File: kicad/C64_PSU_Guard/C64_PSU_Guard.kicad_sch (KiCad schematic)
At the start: 46 parts, among them J1 PSU_IN, J2 DRIVE, J3 UFI_LINK, Q1 AO3401A, Q2 2N7002, Q3 AO3401A, Q4 2N7002, U1 TPS25921ADR, U2 TPS25921ADR

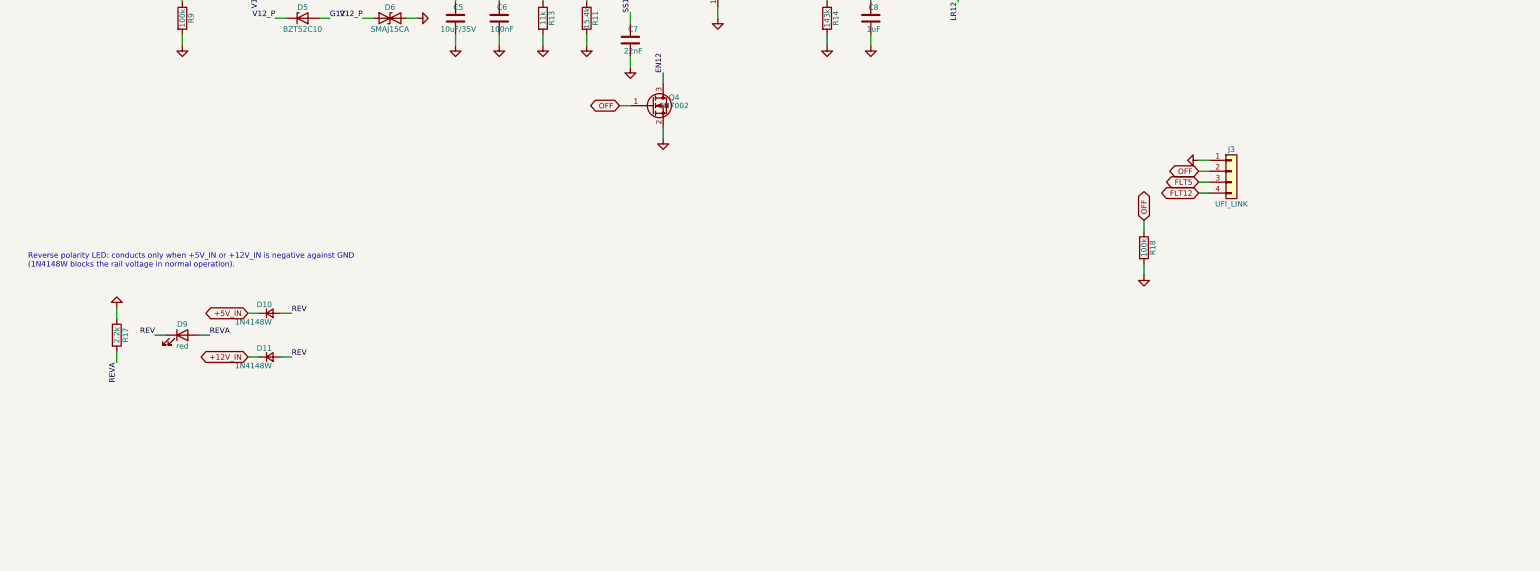
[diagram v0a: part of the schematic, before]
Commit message: C64 PSU Guard: external LED header J4 (2x5, one pair per LED with own series resistor R19-R23, parallel to the on-board LEDs), J3 ERR5/ERR12 now open-drain outputs through 2N7002 inverters Q5/Q6 (the eFuse FLT nodes sit at rail voltage via the red LED chains, up to 12 V, so they must not reach a 3.3 V input directly; high = fault or guard unpowered), README: mapping to UFI Headless J9 (PB6/PB7 with their 2.2k pull-ups, PE0 as OFF); headers 0.5/1 mm off the edge, island vias for pour fragments, GND single-spoke rule for all GND pads, 40 router passes; ERC/DRC 0, fab files regenerated
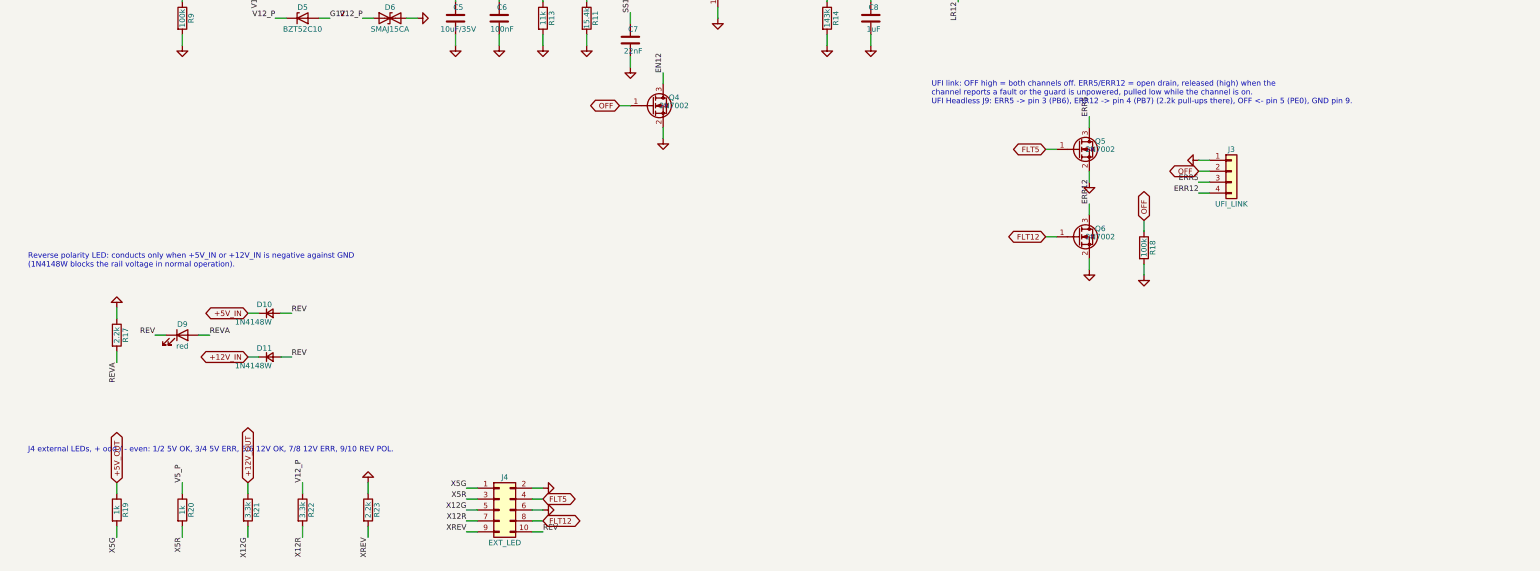
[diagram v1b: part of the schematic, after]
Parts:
- added J4: EXT_LED, Connector_PinHeader_2.54mm:PinHeader_2x05_P2.54mm_Vertical, symbol Connector_Generic:Conn_02x05_Odd_Even
- added Q5, Q6: 2N7002, Package_TO_SOT_SMD:SOT-23, symbol Transistor_FET:2N7002
- added R19, R20: 1k, Resistor_SMD:R_0603_1608Metric, symbol Device:R
- added R21, R22: 3.3k, Resistor_SMD:R_0603_1608Metric, symbol Device:R
- added R23: 2.2k, Resistor_SMD:R_0603_1608Metric, symbol Device:R
- J3: Note reserve: OFF high = both channels off (100k pull-down), FLT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 -> 1 GND, 2 OFF (high = both channels off, 100k pull-down), 3 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
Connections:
- net +12V_OUT: now also R21.1
- net +5V_OUT: now also R19.1
- net FLT12: now also J4.8 (Pin_8), Q6.1 (G); no longer J3.4 (Pin_4)
- net FLT5: now also J4.4 (Pin_4), Q5.1 (G); no longer J3.3 (Pin_3)
- net GND: now also J4.2 (Pin_2), J4.6 (Pin_6), Q5.2 (S), Q6.2 (S), R23.1
- net REV: now also J4.10 (Pin_10)
- net V12_P: now also R22.1
- net V5_P: now also R20.1
- new net ERR12: J3.4 (Pin_4), Q6.3 (D)
- new net ERR5: J3.3 (Pin_3), Q5.3 (D)
- new net X12G: J4.5 (Pin_5), R21.2
- new net X12R: J4.7 (Pin_7), R22.2
- new net X5G: J4.1 (Pin_1), R19.2
- new net X5R: J4.3 (Pin_3), R20.2
- new net XREV: J4.9 (Pin_9), R23.2
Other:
- note added: "J4 external LEDs, + odd / - even: 1/2 5V OK, 3/4 5V ERR, 5/6 12V OK, 7/8 12V ERR, 9/10 REV POL."
- note added: "UFI link: OFF high = both channels off. ERR5/ERR12 = open drain, released (high) when the channel reports a fault or the guard is unpowered, pulled low while the channel is on. UFI Headless J9: ERR5 -> pin 3 (PB6), ERR12 -> pin 4 (PB7) (2.2k pull-ups there), OFF <- pin 5 (PE0), GND pin 9."

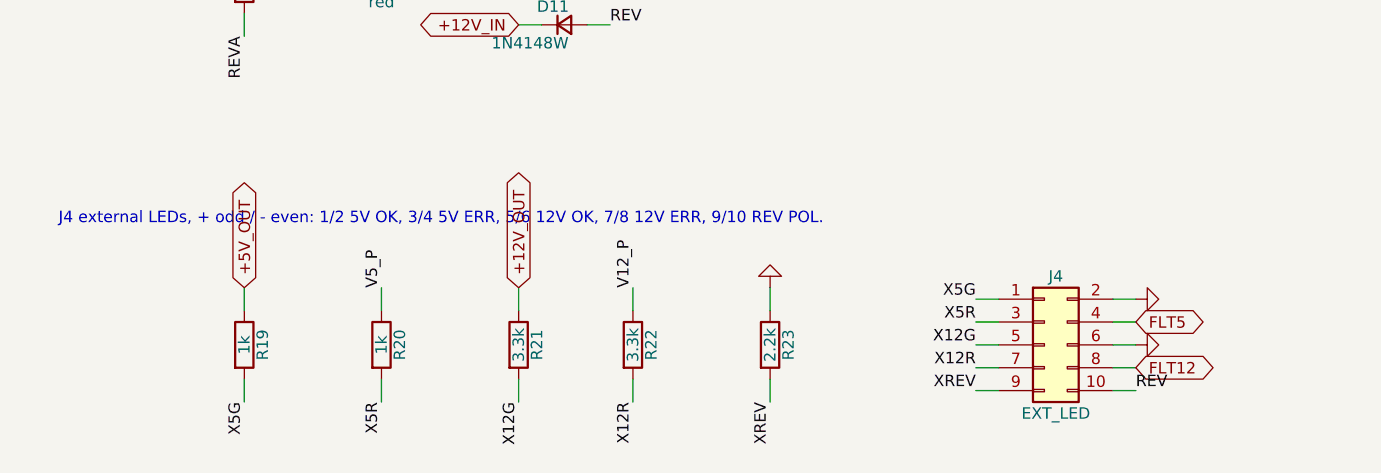
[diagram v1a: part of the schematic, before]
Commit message: C64 PSU Guard: one external fault LED instead of the 2x5 LED header - J4 1x2 (1 = +, 2 = -), 1k from the protected 5 V input, cathode through a 1N4148W diode OR (D12/D13) into both eFuse FLT outputs: on while either channel is switched off; README, fab files regenerated, ERC/DRC 0
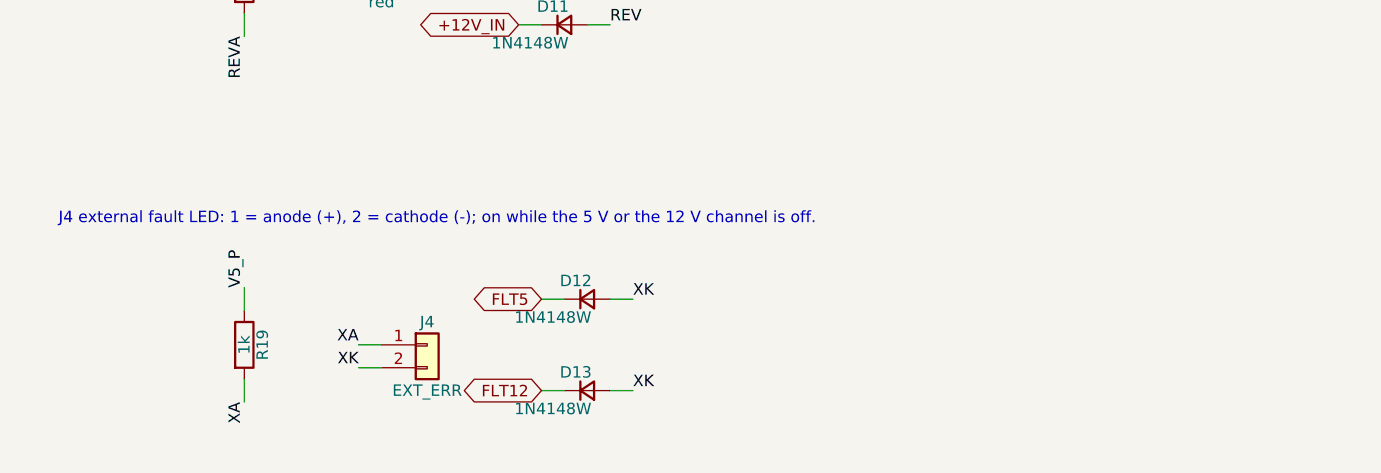
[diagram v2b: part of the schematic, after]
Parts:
- removed R20: 1k, Resistor_SMD:R_0603_1608Metric, symbol Device:R
- removed R21, R22: 3.3k, Resistor_SMD:R_0603_1608Metric, symbol Device:R
- removed R23: 2.2k, Resistor_SMD:R_0603_1608Metric, symbol Device:R
- added D12, D13: 1N4148W, Diode_SMD:D_SOD-123, symbol Device:D_Small
- J4: value EXT_LED -> EXT_ERR; footprint Connector_PinHeader_2.54mm:PinHeader_2x05_P2.54mm_Vertical -> Connector_PinHeader_2.54mm:PinHeader_1x02_P2.54mm_Vertical; symbol Connector_Generic:Conn_02x05_Odd_Even -> Connector_Generic:Conn_01x02; LCSC C2894971 -> C54620389; Note external LEDs, + odd / - even: 5V OK, 5V ERR, 12V OK, 12V E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 -> external fault LED, 1 = + (anode), 2 = - (cathode), ~2.5 mA
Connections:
- net +5V_OUT: no longer R19.1
- net FLT12: now also D13.1 (K); no longer J4.8 (Pin_8)
- net FLT5: now also D12.1 (K); no longer J4.4 (Pin_4)
- net GND: no longer J4.2 (Pin_2), J4.6 (Pin_6)
- net REV: no longer J4.10 (Pin_10)
- net V5_P: now also R19.1
- removed net X12G: J4.5 (Pin_5)
- removed net X12R: J4.7 (Pin_7)
- net X5G renamed XA
- removed net X5R: J4.3 (Pin_3)
- removed net XREV: J4.9 (Pin_9)
- new net XK: D12.2 (A), D13.2 (A), J4.2 (Pin_2)
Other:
- note added: "J4 external fault LED: 1 = anode (+), 2 = cathode (-); on while the 5 V or the 12 V channel is off."
- note removed: "J4 external LEDs, + odd / - even: 1/2 5V OK, 3/4 5V ERR, 5/6 12V OK, 7/8 12V ERR, 9/10 REV POL."

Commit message: C64 PSU Guard v0.2 stage G1 (schematic), review of 2026-10-24: (1) J1 PSU IN is a keyed JST XH B4B-XH-A (LCSC C144395, pin order 1 +5V, 2/3 GND, 4 +12V as on UFI J17/J3) instead of the unkeyed pin header that could be plugged 180 deg rotated (12 V on the 5 V channel, D2 SMF5.0CA would burn); D2 stays the 5 V clamp. (2) D6 SMAJ15CA (VC 24.4 V, above the TPS25921A IN rating 20 V / 22 V for 10 ms) replaced by the unidirectional SMAJ13A (Diodes SMAJ13A-13-F, C110519: VRWM 13 V, VBR 14.4-15.9 V at 1 mA, VC 21.5 V at 18.6 A), drawn as D_Zener so the polarity is visible: pin 1 = cathode = V12_P, pin 2 = GND, D_SMA pad 1 = cathode band. (4) R20/R21 100k (C25803) from FLT5 to V5_P and FLT12 to V12_P, parallel to the red LED chains, so FLT and the Q5/Q6 gates have a defined level; numbered last, v0.1 references unchanged. (5) J3 UFI link is a JST XH B4B-XH-A as well, pin order 1 GND, 2 OFF, 3 ERR5, 4 ERR12 = UFI v1.0 J20 GUARD (netlist of kicad/UFI_Headless: J20.1 GND, J20.2 GUARD_OFF_J <- PG7, J20.3 GUARD_ERR5_J -> PG8, J20.4 GUARD_ERR12_J -> PC9), 1:1 XH cable; schematic notes now name J20 instead of the removed J9. PLAN.md with the stages G1-G3. ERC --severity-all 0 errors / 0 warnings. The board follows in stage G2 (layout regenerated from the scripts), so no DRC in this stage.
Claude-Session: https://claude.ai/code/session_014MdzrcyXuayppPHbfEjUrw
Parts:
- added R20, R21: 100k, Resistor_SMD:R_0603_1608Metric, symbol Device:R
- D6: value SMAJ15CA -> SMAJ13A; symbol Device:D_TVS -> Device:D_Zener; LCSC C110044 -> C110519; MPN (none) -> Diodes SMAJ13A-13-F (unidirectional TVS, VRWM 13 V, VC 21.5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
- J1: footprint Connector_PinHeader_2.54mm:PinHeader_1x04_P2.54mm_Vertical -> Connector_JST:JST_XH_B4B-XH-A_1x04_P2.50mm_Vertical; LCSC C32713270 -> C144395; MPN (none) -> JST B4B-XH-A(LF)(SN) (XH 2.5 mm, 3 A, keyed); Note PC PSU floppy (Berg) plug: 1 +5V red, 2/3 GND black, 4 +12V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 -> keyed XH housing on the adapter cable, Berg pin order 1:1: 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
- J3: footprint Connector_PinHeader_2.54mm:PinHeader_1x04_P2.54mm_Vertical -> Connector_JST:JST_XH_B4B-XH-A_1x04_P2.50mm_Vertical; LCSC C32713270 -> C144395; MPN (none) -> JST B4B-XH-A(LF)(SN) (XH 2.5 mm, 3 A, keyed); Note 1 GND, 2 OFF (high = both channels off, 100k pull-down), 3 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 -> 1:1 XH cable to UFI J20: 1 GND, 2 OFF (high = both channels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
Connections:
- net FLT12: now also R21.2
- net FLT5: now also R20.2
- net V12_P: now also R21.1
- net V5_P: now also R20.1
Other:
- note added: "C64 PSU GUARD - protected 5 V / 12 V feed for a 1541-II / 1581 drive from a PC power supply. v0.2 2026-10-26: J1 PSU in = JST XH B4B-XH-A, keyed (1 +5V, 2/3 GND, 4 +12V; Berg <-> XH adapter cable) -> J2 drive out (DIN pin 1 = 5V, 2 = GND, 4 = 12V). Channel 5 V: limit 1.2 A, OVP 6.0 V, UVLO 4.2 V. Channel 12 V: limit 1.5 A, OVP 14.0 V, UVLO 10.4 V. TPS25921A = auto retry: red LED on while the chan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"
- note added: "FLT pull-ups (v0.2): 100k FLT5 -> V5_P, 100k FLT12 -> V12_P (TPS25921A FLT: open drain, 20 V max)."
- note added: "UFI link: OFF high = both channels off. ERR5/ERR12 = open drain, released (high) when the channel reports a fault or the guard is unpowered, pulled low while the channel is on. UFI Headless v1.0 J20 GUARD (1:1 XH cable): 1 GND, 2 OFF <- PG7 (220R), 3 ERR5 -> PG8, 4 ERR12 -> PC9 (10k pull-ups to 3.3 V, 220R series resistors and PESD3V3L1BA on the UFI side)."
- note removed: "C64 PSU GUARD - protected 5 V / 12 V feed for a 1541-II / 1581 drive from a PC power supply. J1 PSU in (Berg: 1 +5V, 2/3 GND, 4 +12V) -> J2 drive out (DIN pin 1 = 5V, 2 = GND, 4 = 12V). Channel 5 V: limit 1.2 A, OVP 6.0 V, UVLO 4.2 V. Channel 12 V: limit 1.5 A, OVP 14.0 V, UVLO 10.4 V. TPS25921A = auto retry: red LED on while the channel is off, off again when the fault is gone. J3 UFI link (rese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"
- note removed: "UFI link: OFF high = both channels off. ERR5/ERR12 = open drain, released (high) when the channel reports a fault or the guard is unpowered, pulled low while the channel is on. UFI Headless J9: ERR5 -> pin 3 (PB6), ERR12 -> pin 4 (PB7) (2.2k pull-ups there), OFF <- pin 5 (PE0), GND pin 9."

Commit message: C64 PSU Guard v0.2 stage G2 (layout), review finding 3 and the new parts: the load nets are net class Load (1.0 mm, vias 0.8/0.4) in .kicad_pro: +5V_IN, +12V_IN, /V5_P, /V12_P, +5V_OUT, +12V_OUT. Root cause of the 0.25 mm intermediate nodes in v0.1: build_pcb.py assigned the pattern "V5_P"/"V12_P", but the local nets are named "/V5_P"/"/V12_P", so they fell into the default class. The main load paths are now pre-routed in build_pcb.py as locked 1.0 mm F.Cu tracks (Freerouting keeps them): J1 -> Q drain, Q source -> TVS -> 10 uF -> 100 nF -> U IN, U OUT -> 1 uF -> J2; only +5V_OUT changes to B.Cu behind C4, through a locked via pair. finish_pcb.py restores 1.0 mm on Freerouting-necked Load segments where the clearance allows (2 widened this run, 0 left narrow). Placement: J1 and J3 JST XH B4B-XH-A footprints (J1 rot 270, pin 1 +5V at the top; J3 pin 1 GND left), REV-POL group R17/D9/D10/D11 moved right of the wider J1 housing, R20/R21 next to the channel dividers. Silkscreen: back "C64 PSU Guard v0.2 2026-10-26" plus the J3 = UFI J20 pin legend, front "UFI J20", J1 pin labels moved clear of the XH outline. D6 field "Description" moved to "Note" (parity). make_pcb.sh: 4 re-route rounds for leftover connections. New routing_rules.json (min_width 1.0 on all six load nets, min_vias 2 on +5V_OUT, 16 paths covering every hop incl. the intermediate nodes). Gates: ERC --severity-all 0/0; DRC --severity-all --schematic-parity 0 violations / 0 unconnected / 0 parity; check_routing.py exit 0, 0 FEHLER, 0 HALS, every path OK at >= 1.0 mm: 5 V J1->Q1 12.2 mm ~6 mOhm, Q1->U1 IN 19.0 mm ~9 mOhm (v0.1 16.8 mm ~34 mOhm), U1 OUT->C4 3.4 mm, C4->J2 23.4 mm ~11 mOhm; 12 V J1->Q3 12.2 mm, Q3->U2 IN 19.0 mm ~9 mOhm (v0.1 26.4 mm ~52 mOhm), U2 OUT->C8 3.4 mm, C8->J2 28.3 mm ~14 mOhm. Branch connections of the load nets (dividers, LED / pull-up resistors, <= 3 mA) are Freerouting tracks at 1.0 mm, two of them change layer through single vias (+5V_OUT -> R7: one via, +12V_OUT -> R15: a B.Cu 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
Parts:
- D6: Note (none) -> unidirectional TVS, cathode (pin 1) to the 12 V rail
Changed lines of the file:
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@@
 (property "LCSC" "C110519" (at 104.14 185.42 0) (effects (font (size 1.27 1.27)) (hide yes)))
 (property "MPN" "Diodes SMAJ13A-13-F (unidirectional TVS, VRWM 13 V, VC 21.5 V @ 18.6 A)" (at 104.14 185.42 0) (effects (font (size 1.27 1.27)) (hide yes)))
-(property "Description" "Unidirectional TVS, cathode (pin 1) to the 12 V rail" (at 104.14 185.42 0) (effects (font (size 1.27 1.27)) (hide yes)))
+(property "Note" "unidirectional TVS, cathode (pin 1) to the 12 V rail" (at 104.14 185.42 0) (effects (font (size 1.27 1.27)) (hide yes)))
 (pin "1")
 (pin "2")
